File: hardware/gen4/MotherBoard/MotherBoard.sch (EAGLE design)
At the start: 35 parts

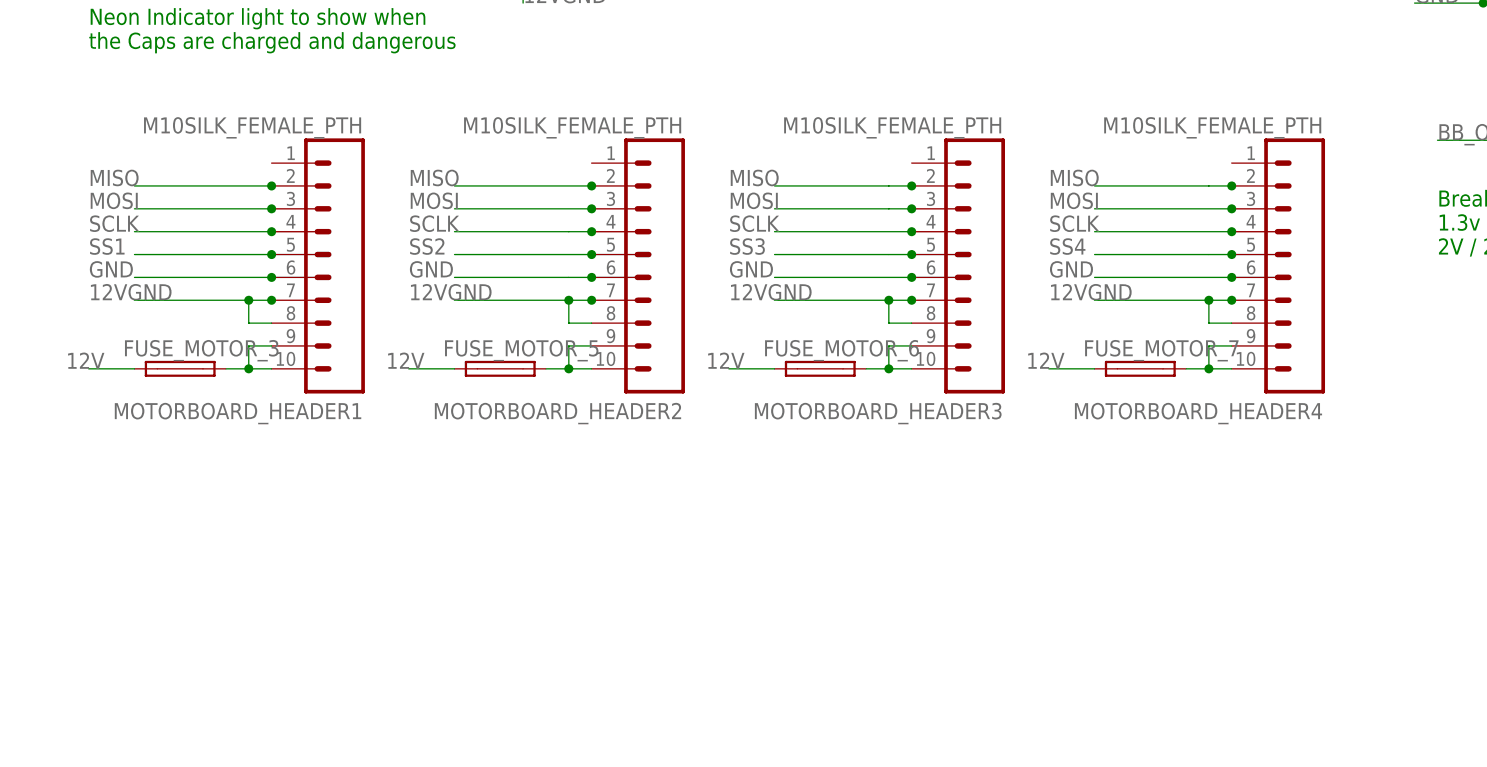
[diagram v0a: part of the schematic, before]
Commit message: added other headers
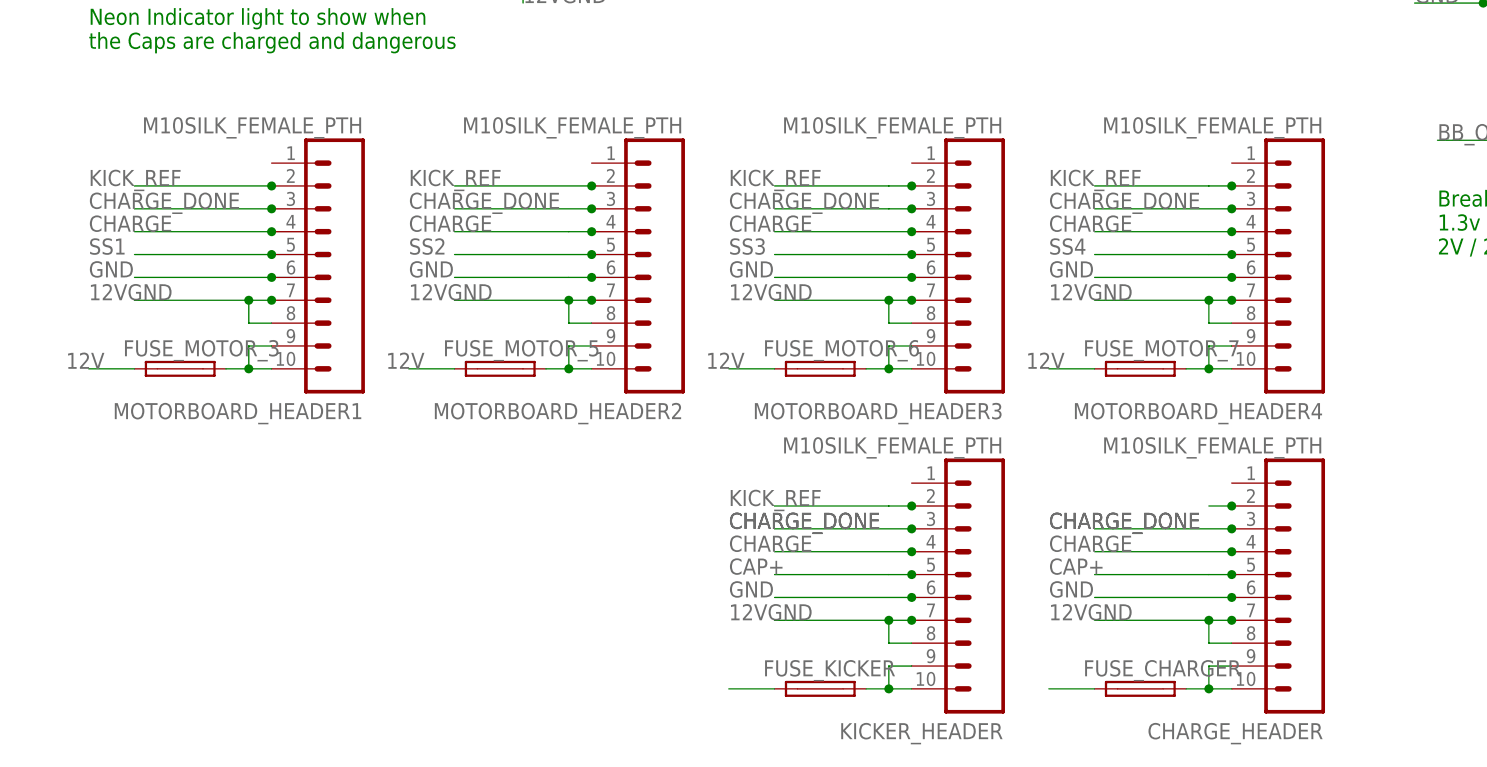
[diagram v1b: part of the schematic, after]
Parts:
- added CHARGE_HEADER, KICKER_HEADER: M10SILK_FEMALE_PTH, SparkFun-Connectors:M10SILK_FEMALE_PTH
- added FUSE_CHARGER, FUSE_KICKER: (no value), fuse:TR5
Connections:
- removed net MISO: MOTORBOARD_HEADER1.2, MOTORBOARD_HEADER2.2, MOTORBOARD_HEADER3.2, MOTORBOARD_HEADER4.2
- removed net MOSI: MOTORBOARD_HEADER1.3, MOTORBOARD_HEADER2.3, MOTORBOARD_HEADER3.3, MOTORBOARD_HEADER4.3
- removed net SCLK: MOTORBOARD_HEADER1.4, MOTORBOARD_HEADER2.4, MOTORBOARD_HEADER3.4, MOTORBOARD_HEADER4.4
- new net 12V1: FUSE_KICKER.1
- new net 12V2: FUSE_CHARGER.1
- new net CHARGE: CHARGE_HEADER.4, KICKER_HEADER.4, MOTORBOARD_HEADER1.4, MOTORBOARD_HEADER2.4, MOTORBOARD_HEADER3.4, MOTORBOARD_HEADER4.4
- new net CHARGE_DONE: CHARGE_HEADER.3, KICKER_HEADER.3, MOTORBOARD_HEADER1.3, MOTORBOARD_HEADER2.3, MOTORBOARD_HEADER3.3, MOTORBOARD_HEADER4.3
- new net KICK_REF: CHARGE_HEADER.2, KICKER_HEADER.2, MOTORBOARD_HEADER1.2, MOTORBOARD_HEADER2.2, MOTORBOARD_HEADER3.2, MOTORBOARD_HEADER4.2
- new net N$10: FUSE_KICKER.2, KICKER_HEADER.10, KICKER_HEADER.9
- new net N$6: CHARGE_HEADER.10, CHARGE_HEADER.9, FUSE_CHARGER.2
- net 12VGND: now also CHARGE_HEADER.7, CHARGE_HEADER.8, KICKER_HEADER.7, KICKER_HEADER.8
- net CAP+: now also CHARGE_HEADER.5, KICKER_HEADER.5
- net GND: now also CHARGE_HEADER.6, KICKER_HEADER.6
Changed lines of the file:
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@@
 <?xml version="1.0" encoding="utf-8"?>
 <!DOCTYPE eagle SYSTEM "eagle.dtd">
-<eagle version="7.2.0">
+<eagle version="7.4.0">
 <drawing>
 <settings>
@@
 <part name="FUSE_MOTOR_6" library="fuse" deviceset="TR5" device=""/>
 <part name="FUSE_MOTOR_7" library="fuse" deviceset="TR5" device=""/>
+<part name="KICKER_HEADER" library="SparkFun-Connectors" deviceset="M10" device="SILK_FEMALE_PTH"/>
+<part name="FUSE_KICKER" library="fuse" deviceset="TR5" device=""/>
+<part name="CHARGE_HEADER" library="SparkFun-Connectors" deviceset="M10" device="SILK_FEMALE_PTH"/>
+<part name="FUSE_CHARGER" library="fuse" deviceset="TR5" device=""/>
 </parts>
 <sheets>
@@
 <attribute name="VALUE" x="90.17" y="-23.241" size="1.778" layer="96"/>
 </instance>
+<instance part="KICKER_HEADER" gate="G$1" x="78.74" y="-50.8" rot="R180"/>
+<instance part="FUSE_KICKER" gate="1" x="58.42" y="-55.88" smashed="yes">
+<attribute name="NAME" x="52.07" y="-54.483" size="1.778" layer="95"/>
+<attribute name="VALUE" x="54.61" y="-58.801" size="1.778" layer="96"/>
+</instance>
+<instance part="CHARGE_HEADER" gate="G$1" x="114.3" y="-50.8" rot="R180"/>
+<instance part="FUSE_CHARGER" gate="1" x="93.98" y="-55.88" smashed="yes">
+<attribute name="NAME" x="87.63" y="-54.483" size="1.778" layer="95"/>
+<attribute name="VALUE" x="90.17" y="-58.801" size="1.778" layer="96"/>
+</instance>
 </instances>
 <busses>
@@
 <junction x="101.6" y="-12.7"/>
 </segment>
+<segment>
+<label x="48.26" y="-48.26" size="1.778" layer="95"/>
+<pinref part="KICKER_HEADER" gate="G$1" pin="7"/>
+<wire x1="68.58" y1="-48.26" x2="66.04" y2="-48.26" width="0.1524" layer="91"/>
+<junction x="68.58" y="-48.26"/>
+<pinref part="KICKER_HEADER" gate="G$1" pin="8"/>
+<wire x1="66.04" y1="-48.26" x2="53.34" y2="-48.26" width="0.1524" layer="91"/>
+<wire x1="68.58" y1="-50.8" x2="66.04" y2="-50.8" width="0.1524" layer="91"/>
+<wire x1="66.04" y1="-50.8" x2="66.04" y2="-48.26" width="0.1524" layer="91"/>
+<junction x="66.04" y="-48.26"/>
+</segment>
+<segment>
+<label x="83.82" y="-48.26" size="1.778" layer="95"/>
+<pinref part="CHARGE_HEADER" gate="G$1" pin="7"/>
+<wire x1="104.14" y1="-48.26" x2="101.6" y2="-48.26" width="0.1524" layer="91"/>
+<junction x="104.14" y="-48.26"/>
+<pinref part="CHARGE_HEADER" gate="G$1" pin="8"/>
+<wire x1="101.6" y1="-48.26" x2="88.9" y2="-48.26" width="0.1524" layer="91"/>
+<wire x1="104.14" y1="-50.8" x2="101.6" y2="-50.8" width="0.1524" layer="91"/>
+<wire x1="101.6" y1="-50.8" x2="101.6" y2="-48.26" width="0.1524" layer="91"/>
+<junction x="101.6" y="-48.26"/>
+</segment>
 </net>
 <net name="BAT+" class="0">
@@
 <label x="124.46" y="20.32" size="1.778" layer="95"/>
 <pinref part="BB_CON" gate="G$1" pin="P$3"/>
+</segment>
+<segment>
+<wire x1="53.34" y1="-45.72" x2="68.58" y2="-45.72" width="0.1524" layer="91"/>
+<label x="48.26" y="-45.72" size="1.778" layer="95"/>
+<pinref part="KICKER_HEADER" gate="G$1" pin="6"/>
+<junction x="68.58" y="-45.72"/>
+</segment>
+<segment>
+<wire x1="88.9" y1="-45.72" x2="104.14" y2="-45.72" width="0.1524" layer="91"/>
+<label x="83.82" y="-45.72" size="1.778" layer="95"/>
+<pinref part="CHARGE_HEADER" gate="G$1" pin="6"/>
+<junction x="104.14" y="-45.72"/>
 </segment>
 </net>
@@
 <label x="-2.54" y="48.26" size="1.778" layer="95"/>
 </segment>
+<segment>
+<label x="48.26" y="-43.18" size="1.778" layer="95"/>
+<pinref part="KICKER_HEADER" gate="G$1" pin="5"/>
+<wire x1="68.58" y1="-43.18" x2="66.04" y2="-43.18" width="0.1524" layer="91"/>
+<junction x="68.58" y="-43.18"/>
+<wire x1="66.04" y1="-43.18" x2="53.34" y2="-43.18" width="0.1524" layer="91"/>
+</segment>
+<segment>
+<label x="83.82" y="-43.18" size="1.778" layer="95"/>
+<pinref part="CHARGE_HEADER" gate="G$1" pin="5"/>
+<wire x1="104.14" y1="-43.18" x2="101.6" y2="-43.18" width="0.1524" layer="91"/>
+<junction x="104.14" y="-43.18"/>
+<wire x1="101.6" y1="-43.18" x2="88.9" y2="-43.18" width="0.1524" layer="91"/>
+</segment>
 </net>
 <net name="TO_NEON" class="0">
@@
 </segment>
 </net>
-<net name="MISO" class="0">
+<net name="KICK_REF" class="0">
 <segment>
 <label x="-22.86" y="0" size="1.778" layer="95"/>
@@
 <wire x1="101.6" y1="0" x2="88.9" y2="0" width="0.1524" layer="91"/>
 </segment>
-</net>
-<net name="MOSI" class="0">
+<segment>
+<label x="48.26" y="-35.56" size="1.778" layer="95"/>
+<pinref part="KICKER_HEADER" gate="G$1" pin="2"/>
+<wire x1="68.58" y1="-35.56" x2="66.04" y2="-35.56" width="0.1524" layer="91"/>
+<junction x="68.58" y="-35.56"/>
+<wire x1="66.04" y1="-35.56" x2="53.34" y2="-35.56" width="0.1524" layer="91"/>
+</segment>
+<segment>
+<pinref part="CHARGE_HEADER" gate="G$1" pin="2"/>
+<wire x1="104.14" y1="-35.56" x2="101.6" y2="-35.56" width="0.1524" layer="91"/>
+<junction x="104.14" y="-35.56"/>
+</segment>
+</net>
+<net name="CHARGE_DONE" class="0">
 <segment>
 <label x="-22.86" y="-2.54" size="1.778" layer="95"/>
@@
 <junction x="104.14" y="-2.54"/>
 </segment>
-</net>
-<net name="SCLK" class="0">
+<segment>
+<label x="48.26" y="-38.1" size="1.778" layer="95"/>
+<pinref part="KICKER_HEADER" gate="G$1" pin="3"/>
+<wire x1="68.58" y1="-38.1" x2="53.34" y2="-38.1" width="0.1524" layer="91"/>
+<junction x="68.58" y="-38.1"/>
+<label x="48.26" y="-38.1" size="1.778" layer="95"/>
+</segment>
+<segment>
+<label x="83.82" y="-38.1" size="1.778" layer="95"/>
+<pinref part="CHARGE_HEADER" gate="G$1" pin="3"/>
+<wire x1="104.14" y1="-38.1" x2="88.9" y2="-38.1" width="0.1524" layer="91"/>
+<junction x="104.14" y="-38.1"/>
+<label x="83.82" y="-38.1" size="1.778" layer="95"/>
+</segment>
+</net>
+<net name="CHARGE" class="0">
 <segment>
 <label x="-22.86" y="-5.08" size="1.778" layer="95"/>
@@
 <junction x="104.14" y="-5.08"/>
 <wire x1="104.14" y1="-5.08" x2="88.9" y2="-5.08" width="0.1524" layer="91"/>
+</segment>
+<segment>
+<label x="48.26" y="-40.64" size="1.778" layer="95"/>
+<pinref part="KICKER_HEADER" gate="G$1" pin="4"/>
+<junction x="68.58" y="-40.64"/>
+<wire x1="68.58" y1="-40.64" x2="53.34" y2="-40.64" width="0.1524" layer="91"/>
+</segment>
+<segment>
+<label x="83.82" y="-40.64" size="1.778" layer="95"/>
+<pinref part="CHARGE_HEADER" gate="G$1" pin="4"/>
+<junction x="104.14" y="-40.64"/>
+<wire x1="104.14" y1="-40.64" x2="88.9" y2="-40.64" width="0.1524" layer="91"/>
 </segment>
 </net>
@@
 </segment>
 </net>
+<net name="12V1" class="0">
+<segment>
+<pinref part="FUSE_KICKER" gate="1" pin="1"/>
+<wire x1="53.34" y1="-55.88" x2="48.26" y2="-55.88" width="0.1524" layer="91"/>
+</segment>
+</net>
+<net name="N$10" class="0">
+<segment>
+<pinref part="KICKER_HEADER" gate="G$1" pin="10"/>
+<pinref part="FUSE_KICKER" gate="1" pin="2"/>
+<wire x1="68.58" y1="-55.88" x2="66.04" y2="-55.88" width="0.1524" layer="91"/>
+<pinref part="KICKER_HEADER" gate="G$1" pin="9"/>
+<wire x1="66.04" y1="-55.88" x2="63.5" y2="-55.88" width="0.1524" layer="91"/>
+<wire x1="68.58" y1="-53.34" x2="66.04" y2="-53.34" width="0.1524" layer="91"/>
+<wire x1="66.04" y1="-53.34" x2="66.04" y2="-55.88" width="0.1524" layer="91"/>
+<junction x="66.04" y="-55.88"/>
+</segment>
+</net>
+<net name="12V2" class="0">
+<segment>
+<pinref part="FUSE_CHARGER" gate="1" pin="1"/>
+<wire x1="88.9" y1="-55.88" x2="83.82" y2="-55.88" width="0.1524" layer="91"/>
+</segment>
+</net>
+<net name="N$6" class="0">
+<segment>
+<pinref part="CHARGE_HEADER" gate="G$1" pin="10"/>
+<pinref part="FUSE_CHARGER" gate="1" pin="2"/>
+<wire x1="104.14" y1="-55.88" x2="101.6" y2="-55.88" width="0.1524" layer="91"/>
+<pinref part="CHARGE_HEADER" gate="G$1" pin="9"/>
+<wire x1="101.6" y1="-55.88" x2="99.06" y2="-55.88" width="0.1524" layer="91"/>
+<wire x1="104.14" y1="-53.34" x2="101.6" y2="-53.34" width="0.1524" layer="91"/>
+<wire x1="101.6" y1="-53.34" x2="101.6" y2="-55.88" width="0.1524" layer="91"/>
+<junction x="101.6" y="-55.88"/>
+</segment>
+</net>

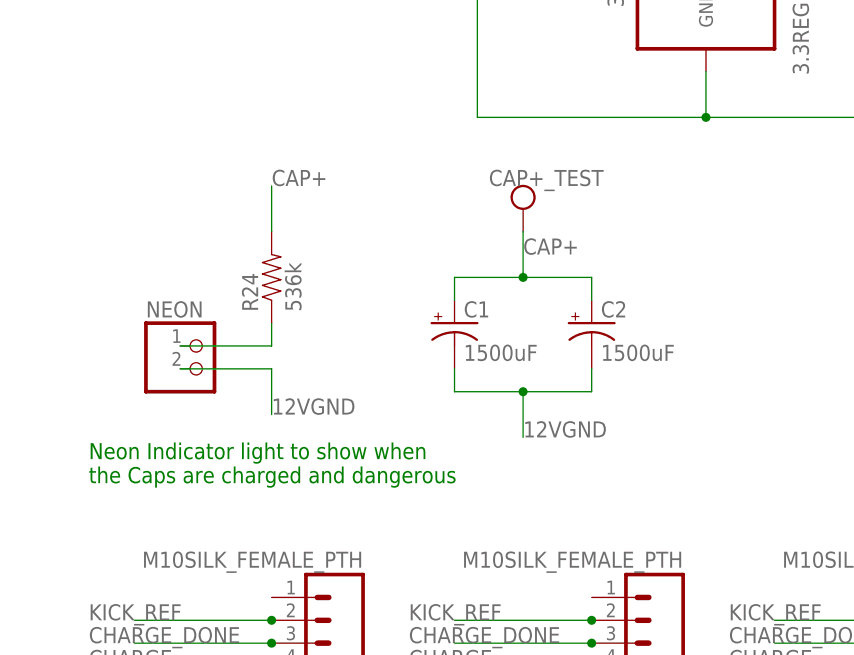
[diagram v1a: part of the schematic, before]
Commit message: combined kicker and charger
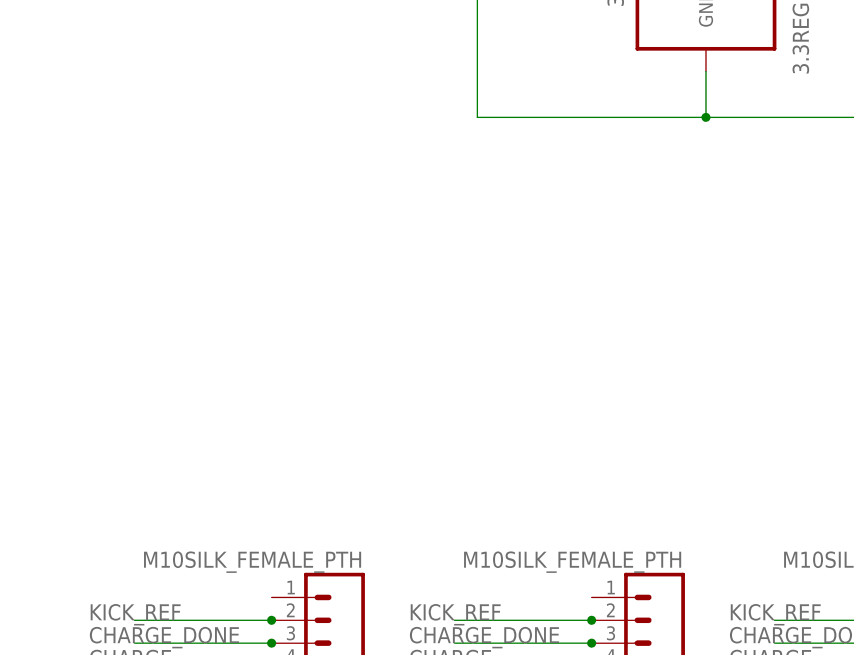
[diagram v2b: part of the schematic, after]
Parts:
- removed C1, C2: 1500uF, rcl:CPOL-USE10-35
- removed CAP+_TEST: TEST_PT, gen3:TEST_PT
- removed NEON: (no value), pinhead:PINHD-1X2
- removed R24: 536k, SparkFun-Passives:RESISTOR0805-RES
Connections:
- removed net TO_NEON: NEON.1, R24.1
- net 12VGND: no longer C1.-, C2.-, NEON.2
- net CAP+: no longer C1.+, C2.+, CAP+_TEST.P$1, R24.2
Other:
- note removed: "Neon Indicator light to show when the Caps are charged and dangerous"
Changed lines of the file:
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@@
 <?xml version="1.0" encoding="utf-8"?>
 <!DOCTYPE eagle SYSTEM "eagle.dtd">
-<eagle version="7.4.0">
+<eagle version="7.5.0">
 <drawing>
 <settings>
@@
 <part name="DRIB_TRAN" library="gen3" deviceset="N-MOSFET" device="DPAK"/>
 <part name="DRIB" library="gen3" deviceset="JST-2" device="2MM"/>
-<part name="C1" library="rcl" deviceset="CPOL-US" device="E10-35" value="1500uF"/>
-<part name="C2" library="rcl" deviceset="CPOL-US" device="E10-35" value="1500uF"/>
-<part name="NEON" library="pinhead" deviceset="PINHD-1X2" device=""/>
-<part name="R24" library="SparkFun-Passives" deviceset="RESISTOR" device="0805-RES" value="536k"/>
 <part name="DRIB_TEST" library="gen3" deviceset="TEST_PT" device=""/>
 <part name="BATSENSE_TEST" library="gen3" deviceset="TEST_PT" device=""/>
-<part name="CAP+_TEST" library="gen3" deviceset="TEST_PT" device=""/>
 <part name="TMP" library="SparkFun-Passives" deviceset="RESISTOR" device="0805-RES" value="0"/>
 <part name="POLARITY_PROTECT" library="diode" deviceset="BAT60J" device=""/>
@@
 <text x="180.34" y="60.96" size="1.778" layer="91">max gate threshold: 2.6V.
 should turn on fine with 3.3!</text>
-<text x="-22.86" y="15.24" size="1.778" layer="91">Neon Indicator light to show when
-the Caps are charged and dangerous</text>
 <text x="127" y="-7.62" size="1.778" layer="91">Breakbeam output:
 1.3v drop, 100mA.
@@
 <instance part="DRIB_TRAN" gate="G$1" x="210.82" y="71.12"/>
 <instance part="DRIB" gate="G$1" x="233.68" y="83.82"/>
-<instance part="C1" gate="G$1" x="17.78" y="33.02"/>
-<instance part="C2" gate="G$1" x="33.02" y="33.02"/>
-<instance part="NEON" gate="G$1" x="-10.16" y="27.94"/>
-<instance part="R24" gate="G$1" x="-2.54" y="38.1" rot="R90"/>
 <instance part="DRIB_TEST" gate="G$1" x="190.5" y="71.12"/>
 <instance part="BATSENSE_TEST" gate="G$1" x="139.7" y="76.2" smashed="yes">
 <attribute name="NAME" x="135.89" y="71.12" size="1.778" layer="95"/>
 </instance>
-<instance part="CAP+_TEST" gate="G$1" x="25.4" y="45.72"/>
 <instance part="TMP" gate="G$1" x="86.36" y="55.88"/>
 <instance part="POLARITY_PROTECT" gate="G$1" x="-7.62" y="83.82" smashed="yes">
@@
 </segment>
 <segment>
-<pinref part="C1" gate="G$1" pin="-"/>
-<wire x1="17.78" y1="27.94" x2="17.78" y2="25.4" width="0.1524" layer="91"/>
-<pinref part="C2" gate="G$1" pin="-"/>
-<wire x1="17.78" y1="25.4" x2="25.4" y2="25.4" width="0.1524" layer="91"/>
-<wire x1="25.4" y1="25.4" x2="33.02" y2="25.4" width="0.1524" layer="91"/>
-<wire x1="33.02" y1="25.4" x2="33.02" y2="27.94" width="0.1524" layer="91"/>
-<junction x="25.4" y="25.4"/>
-<wire x1="25.4" y1="25.4" x2="25.4" y2="20.32" width="0.1524" layer="91"/>
-<label x="25.4" y="20.32" size="1.778" layer="95"/>
-</segment>
-<segment>
-<pinref part="NEON" gate="G$1" pin="2"/>
-<wire x1="-12.7" y1="27.94" x2="-2.54" y2="27.94" width="0.1524" layer="91"/>
-<wire x1="-2.54" y1="27.94" x2="-2.54" y2="22.86" width="0.1524" layer="91"/>
-<label x="-2.54" y="22.86" size="1.778" layer="95"/>
-</segment>
-<segment>
 <label x="-22.86" y="-12.7" size="1.778" layer="95"/>
 <pinref part="MOTORBOARD_HEADER1" gate="G$1" pin="7"/>
@@
 <net name="CAP+" class="0">
 <segment>
-<pinref part="C1" gate="G$1" pin="+"/>
-<wire x1="17.78" y1="35.56" x2="17.78" y2="38.1" width="0.1524" layer="91"/>
-<wire x1="17.78" y1="38.1" x2="25.4" y2="38.1" width="0.1524" layer="91"/>
-<pinref part="C2" gate="G$1" pin="+"/>
-<wire x1="25.4" y1="38.1" x2="33.02" y2="38.1" width="0.1524" layer="91"/>
-<wire x1="33.02" y1="38.1" x2="33.02" y2="35.56" width="0.1524" layer="91"/>
-<wire x1="25.4" y1="38.1" x2="25.4" y2="43.18" width="0.1524" layer="91"/>
-<junction x="25.4" y="38.1"/>
-<label x="25.4" y="40.64" size="1.778" layer="95"/>
-<pinref part="CAP+_TEST" gate="G$1" pin="P$1"/>
-</segment>
-<segment>
-<pinref part="R24" gate="G$1" pin="2"/>
-<wire x1="-2.54" y1="43.18" x2="-2.54" y2="48.26" width="0.1524" layer="91"/>
-<label x="-2.54" y="48.26" size="1.778" layer="95"/>
-</segment>
-<segment>
 <label x="48.26" y="-43.18" size="1.778" layer="95"/>
 <pinref part="KICKER_HEADER" gate="G$1" pin="5"/>
@@
 </segment>
 </net>
-<net name="TO_NEON" class="0">
-<segment>
-<pinref part="R24" gate="G$1" pin="1"/>
-<wire x1="-2.54" y1="33.02" x2="-2.54" y2="30.48" width="0.1524" layer="91"/>
-<pinref part="NEON" gate="G$1" pin="1"/>
-<wire x1="-2.54" y1="30.48" x2="-12.7" y2="30.48" width="0.1524" layer="91"/>
-</segment>
-</net>
